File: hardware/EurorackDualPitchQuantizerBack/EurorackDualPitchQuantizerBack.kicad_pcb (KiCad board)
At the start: 2 copper layers, 48.5 x 110 mm, 41 parts, among them J1 Conn_01x04_Female, J10 Conn_01x02_Female, J2 Conn_01x12_Female, J3 Conn_02x05_Odd_Even, J4 Conn_01x02_Female, J5 MCP4725Breakout, J6 MCP4725Breakout, J7 Conn_01x12_Female, J8 Conn_01x02_Female, J9 Conn_01x01_Female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

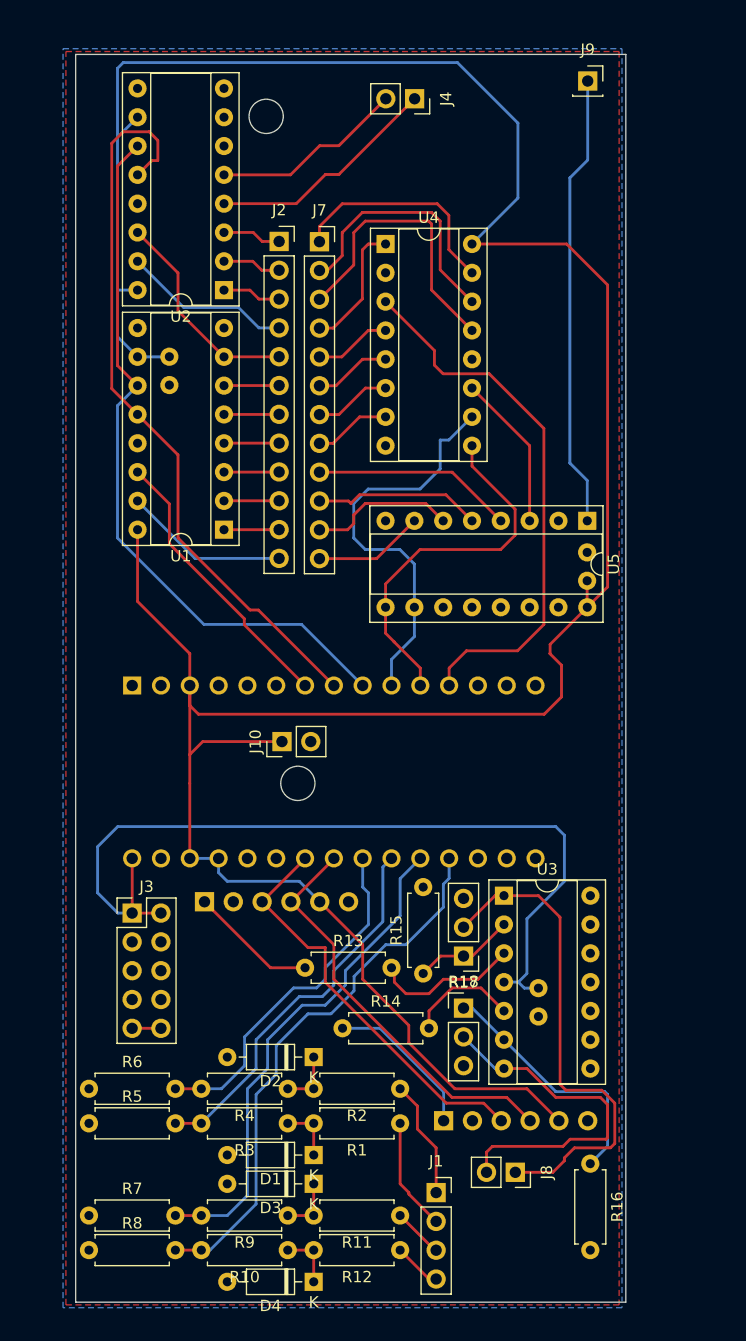
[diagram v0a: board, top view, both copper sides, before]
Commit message: made another version that is not viable since it is too tall
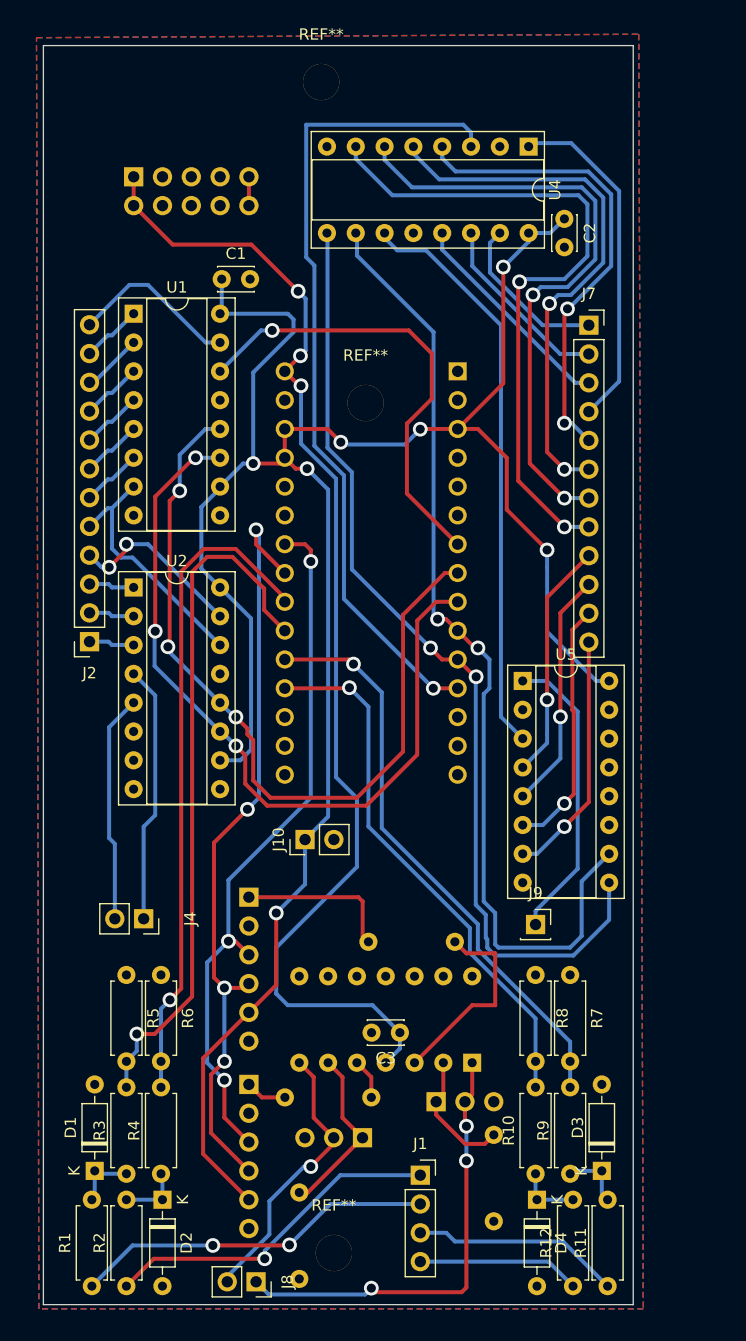
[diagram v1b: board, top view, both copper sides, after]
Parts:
- added REF**: MountingHole_3.2mm_M3, MountingHole:MountingHole_3.2mm_M3, F.Cu at (37.5, 20.2)
- added REF**: MountingHole_3.2mm_M3, MountingHole:MountingHole_3.2mm_M3, F.Cu at (41.4, 48.5)
- added REF**: MountingHole_3.2mm_M3, MountingHole:MountingHole_3.2mm_M3, F.Cu at (38.6, 123.4)
- C1, C2, C3: moved to F.Cu
- J3, R13, R14, R15, R16, R17, R18, U3: moved to B.Cu
- moved J4 76.1 mm to (21.8, 94.0)
- moved J9 74.5 mm to (56.4, 94.5)
- moved J3 64.9 mm to (21.0, 28.6), turned to -90 degrees
- moved R7 47.4 mm to (59.4, 98.9), turned to -90 degrees
- moved R8 46.2 mm to (56.4, 98.9), turned to -90 degrees
- moved C1 41.8 mm to (28.7, 37.6), turned to 0 degrees
- moved A1 39.9 mm to (49.5, 45.7), turned to 180 degrees
- moved J2 39.0 mm to (17.1, 69.6), turned to 180 degrees
- moved C2 36.9 mm to (58.9, 32.3)
- moved R1 30.7 mm to (17.3, 126.4), turned to 90 degrees
- moved R2 29.7 mm to (20.3, 126.4), turned to 90 degrees
- moved U2 27.4 mm to (21.0, 64.8), turned to 0 degrees
- moved R16 25.8 mm to (35.6, 118.1)
- moved D3 25.4 mm to (62.2, 116.2), turned to 90 degrees
- moved R9 25.2 mm to (59.4, 116.5), turned to 90 degrees
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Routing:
- net Net-(U4-Pad7): track 6.79 -> 60.1 mm, vias 0 -> 2
- net Arduino 5V: track 258.4 -> 205.8 mm, vias 0 -> 7
- net Net-(A1-Pad11): track 32.9 -> 85.4 mm, vias 0 -> 2
- net Net-(A1-Pad10): track 36.0 -> 85.2 mm, vias 0 -> 2
- net Net-(U4-Pad6): track 6.79 -> 54.7 mm, vias 0 -> 2
- net Net-(U4-Pad5): track 6.79 -> 48.4 mm, vias 0 -> 2
- net Net-(U4-Pad11): track 13.8 -> 51.1 mm
- net Net-(U4-Pad4): track 6.79 -> 42.0 mm, vias 0 -> 2
- net Net-(A1-Pad23): track 36.3 -> 67.7 mm, vias 0 -> 4
- net +12V: track 75.3 -> 104.3 mm, vias 0 -> 3
- net Net-(A1-Pad21): track 33.8 -> 61.3 mm, vias 0 -> 1
- net Net-(A1-Pad22): track 31.1 -> 58.3 mm, vias 0 -> 1
- net Net-(A1-Pad24): track 36.3 -> 62.3 mm, vias 0 -> 3
- net Net-(A1-Pad12): track 48.1 -> 72.5 mm, vias 0 -> 1
- net Net-(J1-Pad2): track 9.96 -> 32.0 mm, vias 0 -> 2
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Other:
- board size 48.5 x 110 mm -> 52 x 111 mm

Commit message: Got Rev 1.2 complete. It should be manufacturable and fit into eurorack standards.
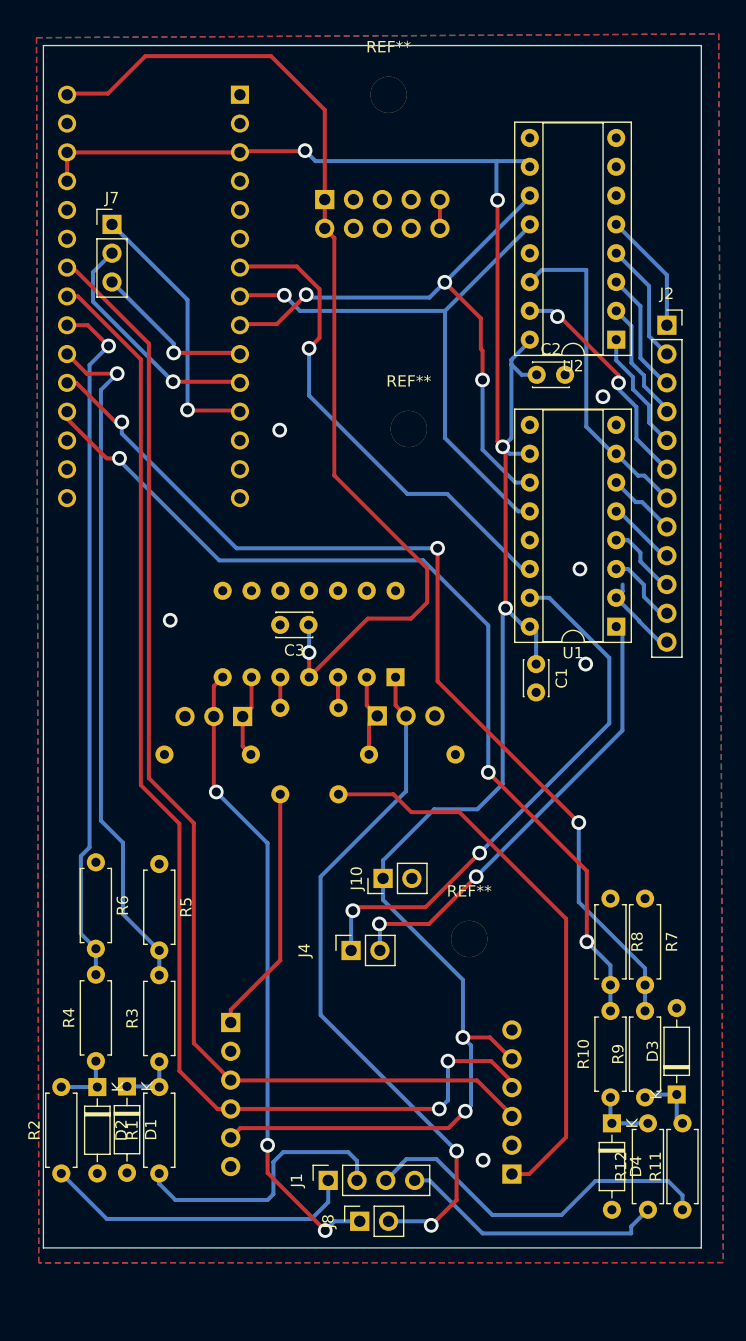
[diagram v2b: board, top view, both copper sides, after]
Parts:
- removed J9: Conn_01x01_Female, Connector_PinSocket_2.54mm:PinSocket_1x01_P2.54mm_Vertical
- removed the REF** at (37.5, 20.2)
- removed the REF** at (41.4, 48.5)
- removed the REF** at (38.6, 123.4)
- removed U4, U5: 4021, Package_DIP:DIP-16_W7.62mm_Socket
- added REF**: MountingHole_3.2mm_M3, MountingHole:MountingHole_3.2mm_M3, F.Cu at (43.4, 21.3)
- added REF**: MountingHole_3.2mm_M3, MountingHole:MountingHole_3.2mm_M3, F.Cu at (50.5, 95.8)
- added REF**: MountingHole_3.2mm_M3, MountingHole:MountingHole_3.2mm_M3, F.Cu at (45.2, 50.8)
- J7: value Conn_01x12_Female -> Conn_01x03_Female; footprint Connector_PinSocket_2.54mm:PinSocket_1x12_P2.54mm_Vertical -> Connector_PinHeader_2.54mm:PinHeader_1x03_P2.54mm_Vertical
- moved J2 58.0 mm to (68.0, 41.7), turned to 0 degrees
- moved U1 50.7 mm to (63.5, 68.2), turned to 180 degrees
- moved U2 47.8 mm to (63.5, 42.9), turned to 180 degrees
- moved C1 43.8 mm to (56.4, 71.5), turned to -90 degrees
- moved J7 43.0 mm to (19.1, 32.8)
- moved R16 38.8 mm to (31.3, 79.5), turned to 180 degrees
- moved R18 38.6 mm to (30.6, 76.1)
- moved C3 36.8 mm to (36.4, 68.1)
- moved R15 35.3 mm to (41.7, 79.5), turned to 0 degrees
- moved U3 34.6 mm to (44.0, 72.7)
- moved R17 34.4 mm to (42.4, 76.1)
- moved J5 33.7 mm to (54.3, 116.5), turned to 0 degrees
- moved A1 31.0 mm to (30.3, 21.3)
- moved R14 26.7 mm to (33.9, 83.0), turned to 90 degrees
- moved J4 18.5 mm to (40.1, 96.8), turned to 90 degrees
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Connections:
- J2 pad 1: /l12 -> /l14
- J2 pad 10: /l3 -> /l5
- J2 pad 11: /l2 -> /l4
- J2 pad 12: /l1 -> /l3
- J2 pad 2: /l11 -> /l13
- J2 pad 3: /l10 -> /l12
- J2 pad 4: /l9 -> /l11
- J2 pad 5: /l8 -> /l10
- J2 pad 6: /l7 -> /l9
- J2 pad 7: /l6 -> /l8
- J2 pad 8: /l5 -> /l7
- J2 pad 9: /l4 -> /l6
- J4 pad 1: /l13 -> /l1
- J4 pad 2: /l14 -> /l2
- J7 pad 1: Net-(U4-Pad15) -> Net-(A1-Pad12)
- J7 pad 2: Net-(U4-Pad14) -> Net-(A1-Pad11)
- J7 pad 3: Net-(U4-Pad13) -> Net-(A1-Pad10)
- J8 pad 1: Net-(J8-Pad1) -> Net-(R18-Pad2)
- R17 pad 2: Net-(J8-Pad1) -> Net-(J8-Pad2)
- R18 pad 2: Net-(J8-Pad2) -> Net-(R18-Pad2)
- U3 pad 1: Net-(J8-Pad1) -> Net-(J8-Pad2)
- U3 pad 7: Net-(J8-Pad2) -> Net-(R18-Pad2)
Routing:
- net Net-(A1-Pad10): track 85.2 -> 14.4 mm, vias 2 -> 1
- net Net-(A1-Pad11): track 85.4 -> 20.9 mm, vias 2 -> 1
- net Net-(U4-Pad7): track 60.1 -> 0.00 mm, vias 2 -> 0
- net Net-(R18-Pad2): track 0.00 -> 56.5 mm, vias 0 -> 3
- net Net-(U4-Pad6): track 54.7 -> 0.00 mm, vias 2 -> 0
- net Net-(U4-Pad11): track 51.1 -> 0.00 mm
- net Net-(A1-Pad12): track 72.5 -> 23.8 mm
- net Net-(U4-Pad5): track 48.4 -> 0.00 mm, vias 2 -> 0
- net Net-(U4-Pad4): track 42.0 -> 0.00 mm, vias 2 -> 0
- net Net-(A1-Pad24): track 62.3 -> 104.1 mm, vias 3 -> 0
- net Net-(A1-Pad23): track 67.7 -> 108.7 mm, vias 4 -> 2
- net Net-(J8-Pad1): track 39.7 -> 0.00 mm, vias 3 -> 0
- net Net-(J8-Pad2): track 24.8 -> 61.6 mm, vias 1 -> 2
- net Net-(A1-Pad20): track 51.4 -> 87.7 mm, vias 1 -> 3
- net Net-(A1-Pad19): track 47.7 -> 83.9 mm, vias 1 -> 3
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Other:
- board size 52 x 111 mm -> 58 x 106 mm
- board text added: "Ilmari Hirvonen DPQ Front Rev 1.2 2022-12-11 CERN-OHL-S v2"

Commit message: minor modifications
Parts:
- moved R16 3.74 mm to (31.1, 83.2)
- moved R15 3.28 mm to (41.7, 82.8)
- moved R17 2.60 mm to (42.7, 78.7)
- moved R18 2.55 mm to (30.1, 78.7)
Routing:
- net Net-(R16-Pad1): track 7.44 -> 11.5 mm
- net Net-(R15-Pad1): track 7.50 -> 11.0 mm
- net Net-(R18-Pad2): track 56.5 -> 59.4 mm
- net Net-(A1-Pad24): track 104.1 -> 105.8 mm
- net Net-(A1-Pad23): track 108.7 -> 110.2 mm
